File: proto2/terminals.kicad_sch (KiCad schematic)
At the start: 216 parts, among them J1 Output 1, J10 Output, J11 Device, J12 Output, J2 Main Power, J3 Output, J4 Output, J5 Device, J6 Output, J7 Device, J8 Output, J9 Device

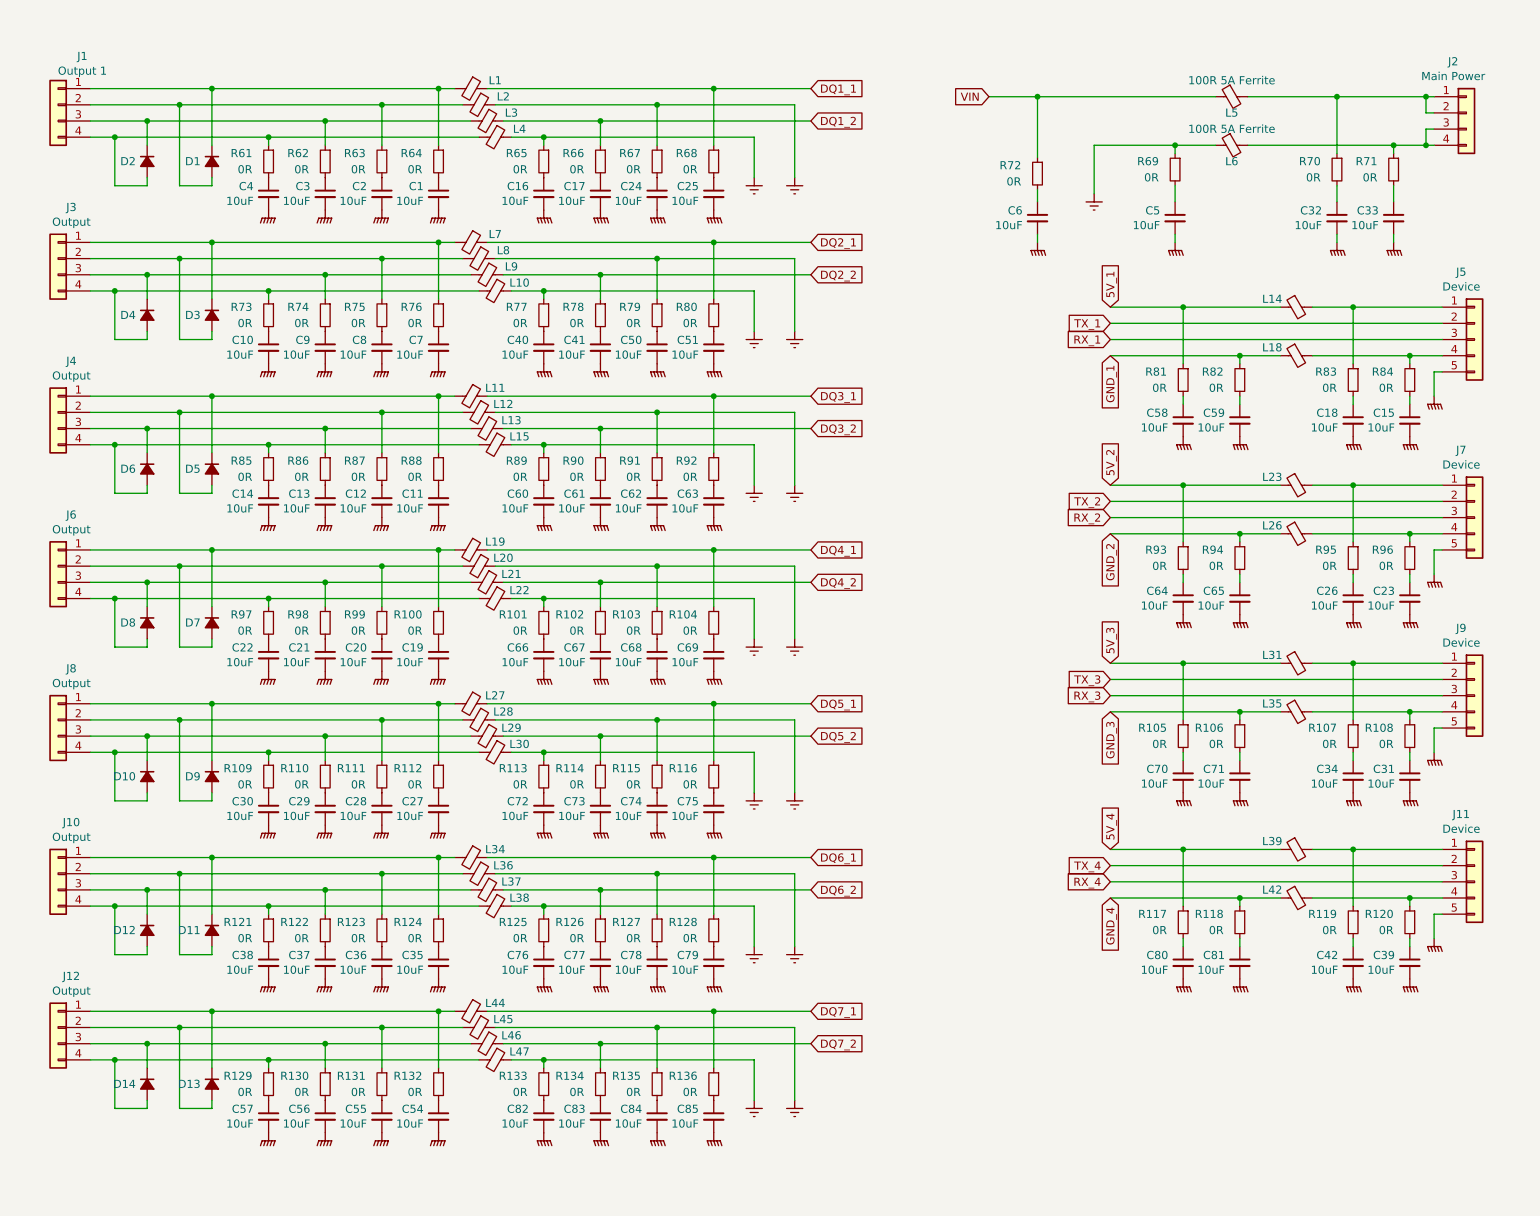
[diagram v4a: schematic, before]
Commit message: Laying out new filters and some schematic updates.
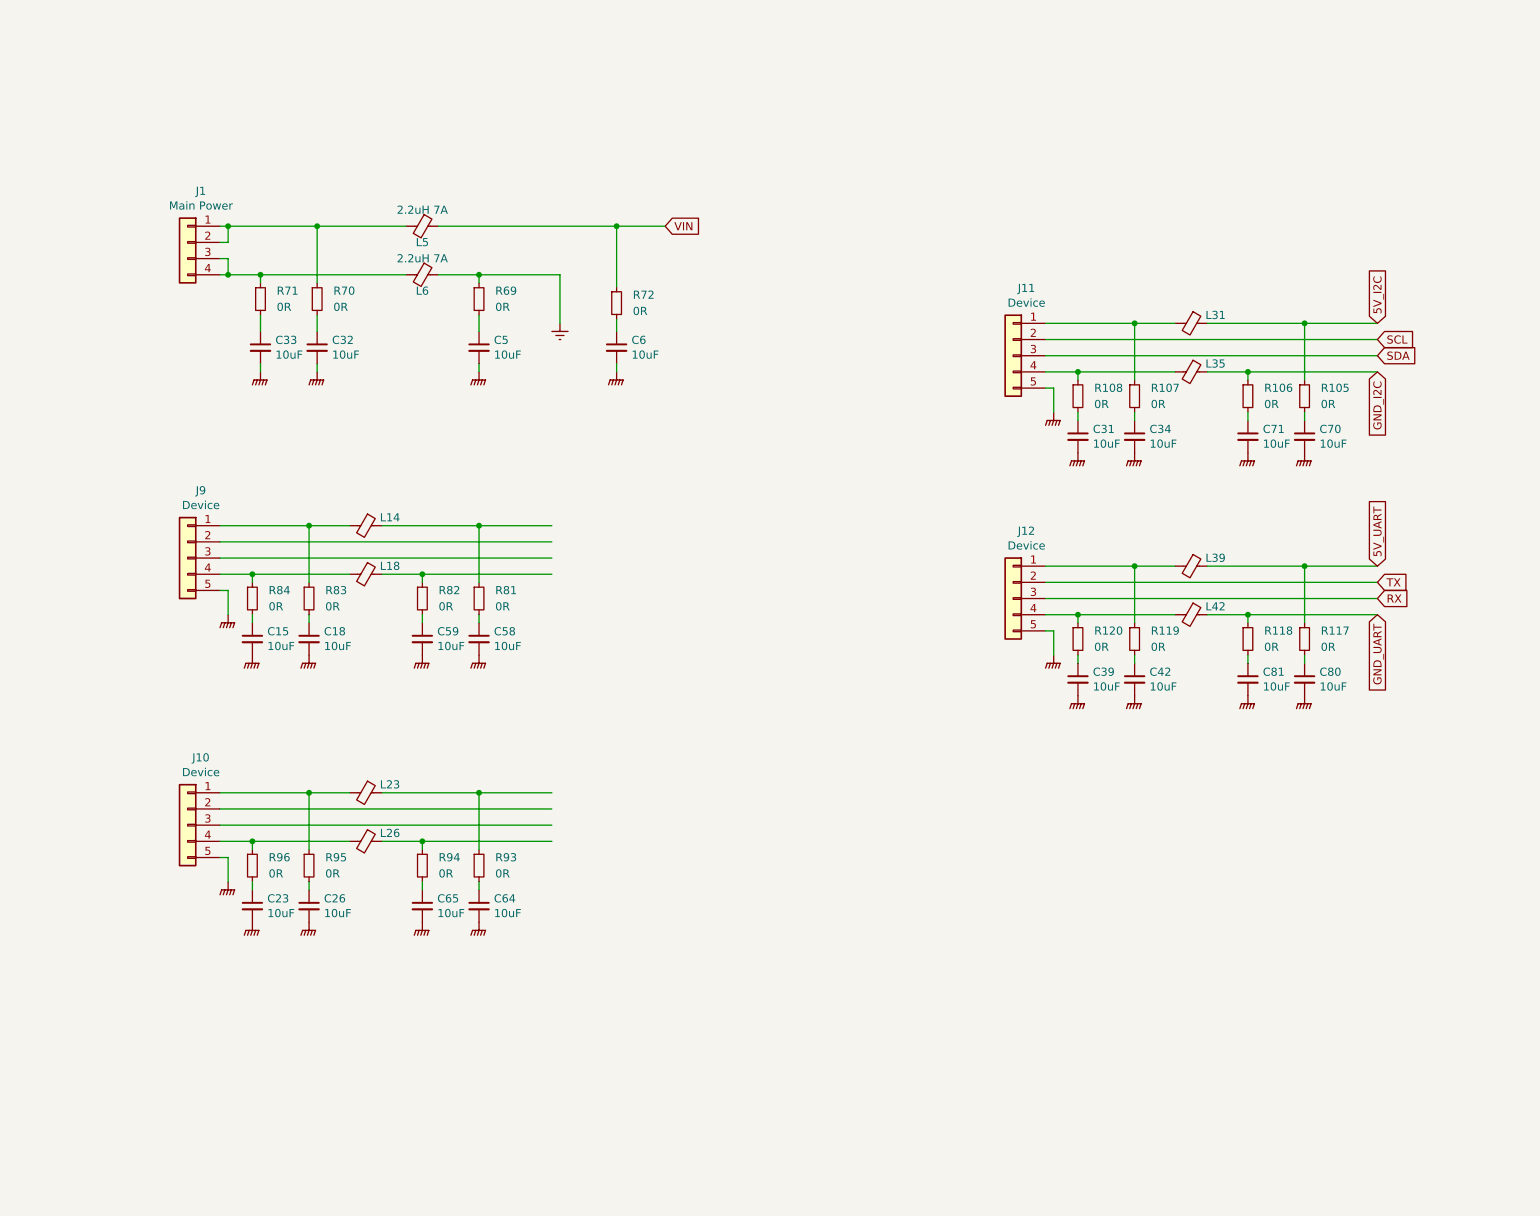
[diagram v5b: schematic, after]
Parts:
- removed C1, C10, C11, C12, C13, C14, C16, C17, C19, C2, C20, C21, C22, C24, C25, C27, C28, C29, C3, C30, C35, C36, C37, C38, C4, C40, C41, C50, C51, C54, C55, C56, C57, C60, C61, C62, C63, C66, C67, C68, C69, C7, C72, C73, C74, C75, C76, C77, C78, C79, C8, C82, C83, C84, C85, C9: 10uF, Capacitor_SMD:C_0805_2012Metric, symbol Device:C_Small
- removed D1, D10, D11, D12, D13, D14, D2, D3, D4, D5, D6, D7, D8, D9: D_Small_ALT, Diode_SMD:D_SOD-123F, symbol Device:D_Small_ALT
- removed J1: Output 1, Connector_BCR:Phoenix_Contact_PST_4, symbol Connector_Generic:Conn_01x04
- removed J10, J12, J3, J4, J6, J8: Output, Connector_BCR:Phoenix_Contact_PST_4, symbol Connector_Generic:Conn_01x04
- removed L1, L10, L11, L12, L13, L15, L19, L2, L20, L21, L22, L27, L28, L29, L3, L30, L34, L36, L37, L38, L4, L44, L45, L46, L47, L7, L8, L9: 10uH 900mA, Inductor_SMD:L_1210_3225Metric, symbol Device:Ferrite_Bead_Small
- removed R100, R101, R102, R103, R104, R109, R110, R111, R112, R113, R114, R115, R116, R121, R122, R123, R124, R125, R126, R127, R128, R129, R130, R131, R132, R133, R134, R135, R136, R61, R62, R63, R64, R65, R66, R67, R68, R73, R74, R75, R76, R77, R78, R79, R80, R85, R86, R87, R88, R89, R90, R91, R92, R97, R98, R99: 0R, Resistor_SMD:R_0805_2012Metric, symbol Device:R_Small
- L14, L18, L23, L26, L31, L35, L39, L42: value 4.7uH 800mA -> 10uH 500mA; footprint Resistor_SMD:R_0805_2012Metric -> Inductor_SMD:L_0805_2012Metric; symbol Device:Ferrite_Bead_Small -> Device:FerriteBead_Small; LCSC C86090 -> C281113; Manufacturer Murata -> Microgate; Part Number LQM21PN4R7MGRD -> MGFL2012F100MT
- L5, L6: value 100R 5A Ferrite -> 2.2uH 7A; symbol Device:Ferrite_Bead_Small -> Device:FerriteBead_Small
- renumbered J2 to J1, J7 to J10, J9 to J11, J11 to J12, J5 to J9
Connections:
- net 5V_1: no longer names the net of L14.1, R81.1
- net 5V_2: no longer names the net of L23.1, R93.1
- net 5V_3 renamed 5V_I2C
- net 5V_4 renamed 5V_UART
- net Earth renamed GND-PWR
- net GNDPWR renamed GND-PE
- net GND_1: no longer names the net of L18.1, R82.1
- net GND_2: no longer names the net of L26.1, R94.1
- net GND_3 renamed GND_I2C
- net GND_4 renamed GND_UART
- net RX_1: no longer names the net of J9.3 (Pin_3)
- net RX_2: no longer names the net of J10.3 (Pin_3)
- net RX_3 renamed SDA
- net RX_4 renamed RX
- net TX_1: no longer names the net of J9.2 (Pin_2)
- net TX_2: no longer names the net of J10.2 (Pin_2)
- net TX_3 renamed SCL
- net TX_4 renamed TX
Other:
- moved on the sheet: C15, C18, C23, C26, C31, C32, C33, C34, C39, C42, C5, C58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

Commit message: Laying out board. in-process commit.
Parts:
- removed C70, C71, C80, C81: 10uF, Capacitor_SMD:C_0805_2012Metric, symbol Device:C_Small
- removed L31, L35: 10uH 500mA, Inductor_SMD:L_0805_2012Metric, symbol Device:FerriteBead_Small
- added C100, C101, C102, C103, C104, C105, C106, C107, C96, C97, C98, C99: 10uF, Capacitor_SMD:C_0805_2012Metric, symbol Device:C_Small
- added L37, L38, L40, L41, L44, L45: 10uH 500mA, Inductor_SMD:L_0805_2012Metric, symbol Device:FerriteBead_Small
- added R150, R151, R152, R153, R154, R155, R156, R157: 0R, Resistor_SMD:R_0805_2012Metric, symbol Device:R_Small
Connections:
- net 5V_I2C: now also L14.1, R108.1; no longer R105.1
- net 5V_UART: now also L23.1, R120.1; no longer L39.1, R117.1
- net GND-PE: now also C100.2, C101.2, C102.2, C103.2, C104.2, C105.2, C106.2, C107.2, C96.2, C97.2, C98.2, C99.2
- net GND-PWR: now also R71.1; no longer R69.1
- net GND_I2C: now also L18.1, R107.1; no longer R106.1
- net GND_UART: now also L26.1, R119.1; no longer L42.1, R118.1
- net at J1.3 (Pin_3), J1.4 (Pin_4), L6.2: now also R69.1; no longer R71.1
- net at C5.1: now also R71.2; no longer R69.2
- net at C31.1: now also R105.2; no longer R108.2
- net at C39.1: now also R119.2; no longer R120.2
- net at C42.1: now also R120.2; no longer R119.2
- net at C26.1: now also R118.2; no longer R95.2
- net at C23.1: now also R117.2; no longer R96.2
- net at C15.1: now also R81.2; no longer R84.2
- net at C18.1: now also R82.2; no longer R83.2
- net at J11.1 (Pin_1): now also L14.2, R106.1; no longer R107.1
- net at J11.4 (Pin_4): now also L18.2, R105.1; no longer R108.1
- net at C34.1: now also R108.2; no longer R107.2
- net at J10.2 (Pin_2): now also L42.2, R152.1
- net at J10.3 (Pin_3): now also L44.2, R151.1
- net 24V_DI1: now reaches R94.1
- net 24V_DI1: now also L39.1, R93.1, R95.1, L38.1, L40.1; no longer L26.1
- net at J9.2 (Pin_2): now also R83.1, L38.2
- net at J9.3 (Pin_3): now also L39.2, R82.1
- net at R81.1: now also J9.4 (Pin_4), L40.2; no longer L14.1
- net at C59.1: now also R84.2; no longer R82.2
- net at C58.1: now also R83.2; no longer R81.2
- net at R94.2: now also C97.1; no longer C65.1
- net at R70.2: now also C65.1; no longer C32.1
- net at C64.1: now also R69.2; no longer R93.2
- net at C33.1: now also R107.2; no longer R71.2
- net at R106.2: now also C32.1
- new net: J12.1 (Pin_1), L23.2, R118.1
- new net: J12.4 (Pin_4), L26.2, R117.1
- new net: J10.1 (Pin_1), L41.2, R153.1
- new net: J10.4 (Pin_4), L45.2, R150.1
- new net: J9.1 (Pin_1), L37.2, R84.1
- new net: C107.1, R157.2
- new net: C99.1, R96.2
- new net: C103.1, R153.2
- new net: C98.1, R95.2
- new net: C105.1, R155.2
- new net: C100.1, R150.2
- new net: C104.1, R154.2
- new net: C106.1, R156.2
- new net: C96.1, R93.2
- new net: C101.1, R151.2
- new net: C102.1, R152.2
- new net 24V_DI2: L42.1, L44.1, L45.1, R154.1, R155.1, R156.1
- new net DI1_1: L37.1, R96.1
- new net DI2_1: L41.1, R157.1
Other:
- moved on the sheet: C15, C18, C23, C26, C32, C33, C34, C39, C42, C58, C59, C64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

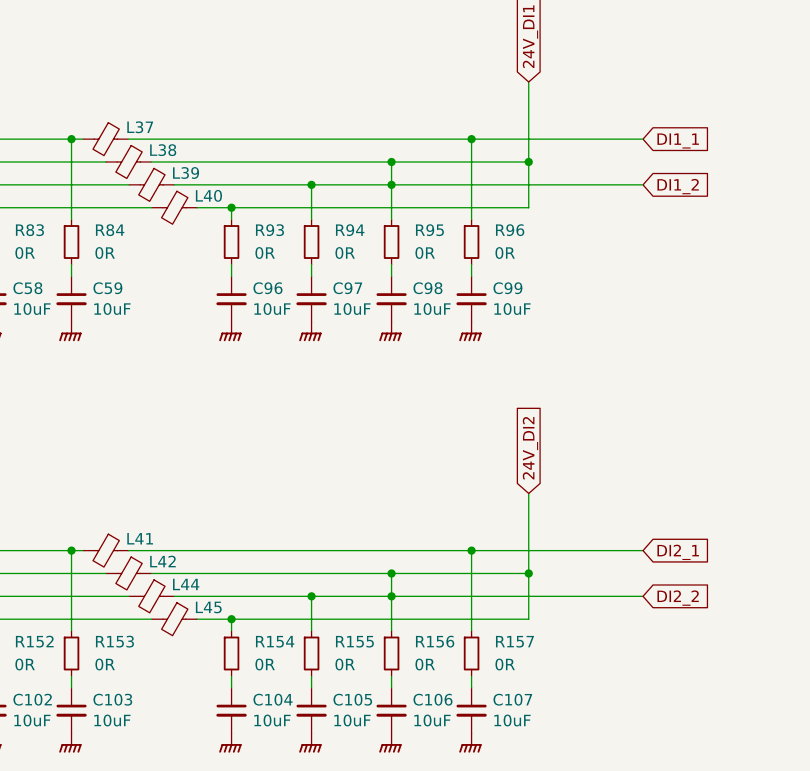
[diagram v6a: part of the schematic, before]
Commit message: Filter layout and some schematic fixes.
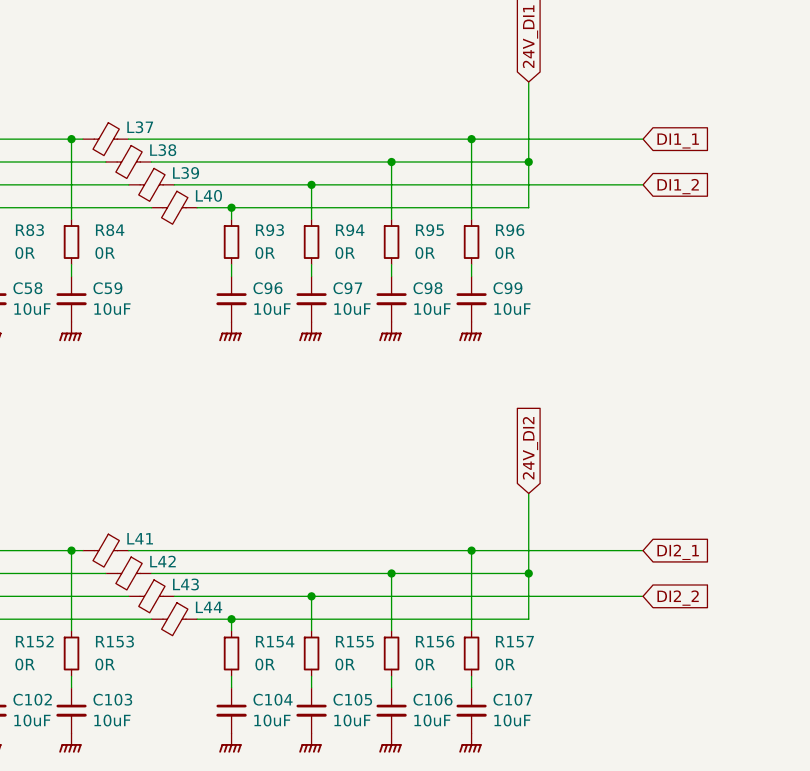
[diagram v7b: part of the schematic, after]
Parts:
- renumbered L44 to L43, L45 to L44
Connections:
- net 24V_DI1: no longer L39.1, R94.1
- net 24V_DI2: no longer L43.1, R155.1
- new net DI1_2: L39.1, R94.1
- new net DI2_2: L43.1, R155.1
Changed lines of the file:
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@@
   (junction (at 127 97.79) (diameter 0) (color 0 0 0 0)
   )
-  (junction (at 111.76 146.05) (diameter 0) (color 0 0 0 0)
-  )
   (junction (at 120.65 140.97) (diameter 0) (color 0 0 0 0)
   )
   (junction (at 93.98 102.87) (diameter 0) (color 0 0 0 0)
   )
-  (junction (at 111.76 100.33) (diameter 0) (color 0 0 0 0)
-  )
   (junction (at 53.34 45.72) (diameter 0) (color 0 0 0 0)
   )
@@
     (stroke (width 0) (type default) (color 0 0 0 0))
   )
-  (wire (pts (xy 111.76 97.79) (xy 111.76 100.33))
-    (stroke (width 0) (type default) (color 0 0 0 0))
-  )
-  (wire (pts (xy 111.76 146.05) (xy 111.76 149.86))
-    (stroke (width 0) (type default) (color 0 0 0 0))
-  )
   (wire (pts (xy 222.25 74.93) (xy 222.25 76.2))
     (stroke (width 0) (type default) (color 0 0 0 0))
@@
     (stroke (width 0) (type default) (color 0 0 0 0))
   )
-  (wire (pts (xy 111.76 146.05) (xy 102.87 146.05))
-    (stroke (width 0) (type default) (color 0 0 0 0))
-  )
   (wire (pts (xy 207.01 68.58) (xy 213.36 68.58))
     (stroke (width 0) (type default) (color 0 0 0 0))
@@
     (stroke (width 0) (type default) (color 0 0 0 0))
   )
-  (wire (pts (xy 111.76 100.33) (xy 111.76 104.14))
+  (wire (pts (xy 111.76 97.79) (xy 111.76 104.14))
     (stroke (width 0) (type default) (color 0 0 0 0))
   )
@@
     (stroke (width 0) (type default) (color 0 0 0 0))
   )
-  (wire (pts (xy 111.76 146.05) (xy 139.7 146.05))
+  (wire (pts (xy 102.87 146.05) (xy 139.7 146.05))
     (stroke (width 0) (type default) (color 0 0 0 0))
   )
@@
     (stroke (width 0) (type default) (color 0 0 0 0))
   )
-  (wire (pts (xy 111.76 143.51) (xy 111.76 146.05))
+  (wire (pts (xy 111.76 143.51) (xy 111.76 149.86))
     (stroke (width 0) (type default) (color 0 0 0 0))
   )
@@
     (stroke (width 0) (type default) (color 0 0 0 0))
   )
-  (wire (pts (xy 111.76 100.33) (xy 139.7 100.33))
-    (stroke (width 0) (type default) (color 0 0 0 0))
-  )
   (wire (pts (xy 111.76 110.49) (xy 111.76 109.22))
     (stroke (width 0) (type default) (color 0 0 0 0))
@@
     (stroke (width 0) (type default) (color 0 0 0 0))
   )
-  (wire (pts (xy 111.76 100.33) (xy 102.87 100.33))
+  (wire (pts (xy 102.87 100.33) (xy 139.7 100.33))
     (stroke (width 0) (type default) (color 0 0 0 0))
   )
@@
   (symbol (lib_id "Device:FerriteBead_Small") (at 87.63 148.59 270) (unit 1)
     (in_bom yes) (on_board yes)
-    (property "Reference" "L45" (id 0) (at 91.44 147.32 90))
+    (property "Reference" "L44" (id 0) (at 91.44 147.32 90))
     (property "Value" "10uH 500mA" (id 1) (at 87.63 144.8816 90)
       (effects (font (size 1.27 1.27)) hide)
@@
   (symbol (lib_id "Device:FerriteBead_Small") (at 85.09 146.05 270) (unit 1)
     (in_bom yes) (on_board yes)
-    (property "Reference" "L44" (id 0) (at 88.9 144.78 90))
+    (property "Reference" "L43" (id 0) (at 88.9 144.78 90))
     (property "Value" "10uH 500mA" (id 1) (at 85.09 142.3416 90)
       (effects (font (size 1.27 1.27)) hide)

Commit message: Final layout for 0.2.0 and various BOM and minor schematic updates.
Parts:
- J1, J10, J11, J12, J9: MPN (none) -> DNP
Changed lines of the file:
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@@
+      (effects (font (size 1.27 1.27)) hide)
+    )
+    (property "MPN" "DNP" (id 4) (at 46.99 48.26 0)
       (effects (font (size 1.27 1.27)) hide)
     )
@@
       (effects (font (size 1.27 1.27)) hide)
     )
-    (property "Datasheet" "~" (id 3) (at 83.82 45.72 0)
+    (property "Datasheet" "https://datasheet.lcsc.com/lcsc/1912111437_COILMX-MS0630-2R2M_C380175.pdf" (id 3) (at 83.82 45.72 0)
       (effects (font (size 1.27 1.27)) hide)
     )
@@
       (effects (font (size 1.27 1.27)) hide)
     )
-    (property "Datasheet" "~" (id 3) (at 83.82 53.34 0)
+    (property "Datasheet" "https://datasheet.lcsc.com/lcsc/1912111437_COILMX-MS0630-2R2M_C380175.pdf" (id 3) (at 83.82 53.34 0)
       (effects (font (size 1.27 1.27)) hide)
     )
@@
       (effects (font (size 1.27 1.27)) hide)
     )
+    (property "MPN" "DNP" (id 4) (at 176.53 104.14 0)
+      (effects (font (size 1.27 1.27)) hide)
+    )
     (pin "1")
     (pin "2")
@@
       (effects (font (size 1.27 1.27)) hide)
     )
+    (property "MPN" "DNP" (id 4) (at 176.53 66.04 0)
+      (effects (font (size 1.27 1.27)) hide)
+    )
     (pin "1")
     (pin "2")
@@
       (effects (font (size 1.27 1.27)) hide)
     )
+    (property "MPN" "DNP" (id 4) (at 39.37 146.05 0)
+      (effects (font (size 1.27 1.27)) hide)
+    )
     (pin "1")
     (pin "2")
@@
       (effects (font (size 1.27 1.27)) hide)
     )
+    (property "MPN" "DNP" (id 4) (at 39.37 100.33 0)
+      (effects (font (size 1.27 1.27)) hide)
+    )
